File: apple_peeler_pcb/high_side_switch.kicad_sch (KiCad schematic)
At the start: 7 parts, among them Q7 2N7002, Q8 AO3401A

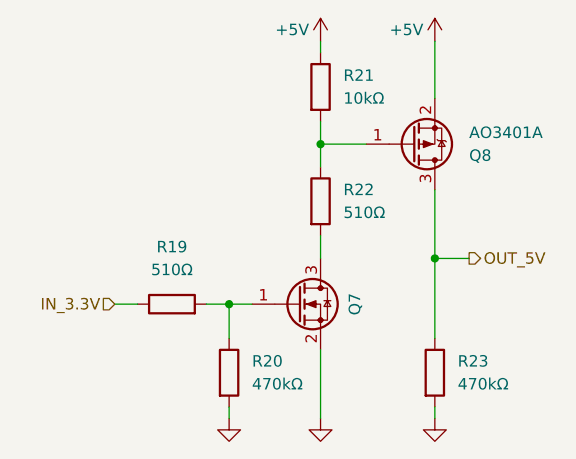
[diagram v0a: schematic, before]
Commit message: we paid for all the pins, we're gonna use all the pins
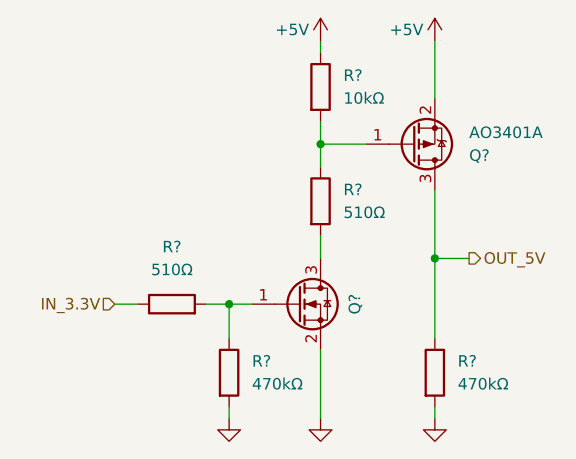
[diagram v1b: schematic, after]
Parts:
- renumbered Q8 to Q?, Q7 to Q?, R21 to R?, R22 to R?, R19 to R?, R23 to R?, R20 to R?
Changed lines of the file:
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@@
 		(on_board yes)
 		(dnp no)
-		(property "Reference" "#PWR044"
+		(property "Reference" "#PWR0106"
 			(at 153.67 128.27 0)
 			(effects
@@
 		(instances
 			(project "apple_peeler_pcb"
-				(path "/d5946b96-44a8-4a28-8641-19803e1510af/ab4760da-4146-4688-a275-418314974b55/6046dcba-ade8-41f9-96d2-caaf24154fd4"
-					(reference "#PWR044")
+				(path "/d5946b96-44a8-4a28-8641-19803e1510af/ab4760da-4146-4688-a275-418314974b55/207d6e2c-5657-4cae-9098-bf31bbf0eeb3/3e7a2019-c147-43be-8925-3656ede786af"
+					(reference "#PWR050")
+					(unit 1)
+				)
+				(path "/d5946b96-44a8-4a28-8641-19803e1510af/ab4760da-4146-4688-a275-418314974b55/216077bc-1e97-451f-9a4f-0a4e0691e85e/3e7a2019-c147-43be-8925-3656ede786af"
+					(reference "#PWR0106")
 					(unit 1)
 				)
@@
 		(on_board yes)
 		(dnp no)
-		(property "Reference" "#PWR043"
+		(property "Reference" "#PWR0105"
 			(at 153.67 83.82 0)
 			(effects
@@
 		(instances
 			(project "apple_peeler_pcb"
-				(path "/d5946b96-44a8-4a28-8641-19803e1510af/ab4760da-4146-4688-a275-418314974b55/6046dcba-ade8-41f9-96d2-caaf24154fd4"
-					(reference "#PWR043")
+				(path "/d5946b96-44a8-4a28-8641-19803e1510af/ab4760da-4146-4688-a275-418314974b55/207d6e2c-5657-4cae-9098-bf31bbf0eeb3/3e7a2019-c147-43be-8925-3656ede786af"
+					(reference "#PWR049")
+					(unit 1)
+				)
+				(path "/d5946b96-44a8-4a28-8641-19803e1510af/ab4760da-4146-4688-a275-418314974b55/216077bc-1e97-451f-9a4f-0a4e0691e85e/3e7a2019-c147-43be-8925-3656ede786af"
+					(reference "#PWR0105")
 					(unit 1)
 				)
@@
 		(dnp no)
 		(fields_autoplaced yes)
-		(property "Reference" "R21"
+		(property "Reference" "R?"
 			(at 143.51 83.8199 0)
 			(effects
@@
 		(instances
 			(project "apple_peeler_pcb"
-				(path "/d5946b96-44a8-4a28-8641-19803e1510af/ab4760da-4146-4688-a275-418314974b55/6046dcba-ade8-41f9-96d2-caaf24154fd4"
-					(reference "R21")
+				(path "/d5946b96-44a8-4a28-8641-19803e1510af/ab4760da-4146-4688-a275-418314974b55/207d6e2c-5657-4cae-9098-bf31bbf0eeb3/3e7a2019-c147-43be-8925-3656ede786af"
+					(reference "R?")
+					(unit 1)
+				)
+				(path "/d5946b96-44a8-4a28-8641-19803e1510af/ab4760da-4146-4688-a275-418314974b55/216077bc-1e97-451f-9a4f-0a4e0691e85e/3e7a2019-c147-43be-8925-3656ede786af"
+					(reference "R?")
 					(unit 1)
 				)
@@
 		(on_board yes)
 		(dnp no)
-		(property "Reference" "#PWR041"
+		(property "Reference" "#PWR0100"
 			(at 140.97 83.82 0)
 			(effects
@@
 		(instances
 			(project "apple_peeler_pcb"
-				(path "/d5946b96-44a8-4a28-8641-19803e1510af/ab4760da-4146-4688-a275-418314974b55/6046dcba-ade8-41f9-96d2-caaf24154fd4"
-					(reference "#PWR041")
+				(path "/d5946b96-44a8-4a28-8641-19803e1510af/ab4760da-4146-4688-a275-418314974b55/207d6e2c-5657-4cae-9098-bf31bbf0eeb3/3e7a2019-c147-43be-8925-3656ede786af"
+					(reference "#PWR044")
+					(unit 1)
+				)
+				(path "/d5946b96-44a8-4a28-8641-19803e1510af/ab4760da-4146-4688-a275-418314974b55/216077bc-1e97-451f-9a4f-0a4e0691e85e/3e7a2019-c147-43be-8925-3656ede786af"
+					(reference "#PWR0100")
 					(unit 1)
 				)
@@
 		(dnp no)
 		(fields_autoplaced yes)
-		(property "Reference" "R22"
+		(property "Reference" "R?"
 			(at 143.51 96.5199 0)
 			(effects
@@
 		(instances
 			(project "apple_peeler_pcb"
-				(path "/d5946b96-44a8-4a28-8641-19803e1510af/ab4760da-4146-4688-a275-418314974b55/6046dcba-ade8-41f9-96d2-caaf24154fd4"
-					(reference "R22")
+				(path "/d5946b96-44a8-4a28-8641-19803e1510af/ab4760da-4146-4688-a275-418314974b55/207d6e2c-5657-4cae-9098-bf31bbf0eeb3/3e7a2019-c147-43be-8925-3656ede786af"
+					(reference "R?")
+					(unit 1)
+				)
+				(path "/d5946b96-44a8-4a28-8641-19803e1510af/ab4760da-4146-4688-a275-418314974b55/216077bc-1e97-451f-9a4f-0a4e0691e85e/3e7a2019-c147-43be-8925-3656ede786af"
+					(reference "R?")
 					(unit 1)
 				)
@@
 		(dnp no)
 		(fields_autoplaced yes)
-		(property "Reference" "R19"
+		(property "Reference" "R?"
 			(at 124.46 102.87 90)
 			(effects
@@
 		(instances
 			(project "apple_peeler_pcb"
-				(path "/d5946b96-44a8-4a28-8641-19803e1510af/ab4760da-4146-4688-a275-418314974b55/6046dcba-ade8-41f9-96d2-caaf24154fd4"
-					(reference "R19")
+				(path "/d5946b96-44a8-4a28-8641-19803e1510af/ab4760da-4146-4688-a275-418314974b55/207d6e2c-5657-4cae-9098-bf31bbf0eeb3/3e7a2019-c147-43be-8925-3656ede786af"
+					(reference "R?")
+					(unit 1)
+				)
+				(path "/d5946b96-44a8-4a28-8641-19803e1510af/ab4760da-4146-4688-a275-418314974b55/216077bc-1e97-451f-9a4f-0a4e0691e85e/3e7a2019-c147-43be-8925-3656ede786af"
+					(reference "R?")
 					(unit 1)
 				)
@@
 		(on_board yes)
 		(dnp no)
-		(property "Reference" "#PWR042"
+		(property "Reference" "#PWR0101"
 			(at 140.97 128.27 0)
 			(effects
@@
 		(instances
 			(project "apple_peeler_pcb"
-				(path "/d5946b96-44a8-4a28-8641-19803e1510af/ab4760da-4146-4688-a275-418314974b55/6046dcba-ade8-41f9-96d2-caaf24154fd4"
-					(reference "#PWR042")
+				(path "/d5946b96-44a8-4a28-8641-19803e1510af/ab4760da-4146-4688-a275-418314974b55/207d6e2c-5657-4cae-9098-bf31bbf0eeb3/3e7a2019-c147-43be-8925-3656ede786af"
+					(reference "#PWR048")
+					(unit 1)
+				)
+				(path "/d5946b96-44a8-4a28-8641-19803e1510af/ab4760da-4146-4688-a275-418314974b55/216077bc-1e97-451f-9a4f-0a4e0691e85e/3e7a2019-c147-43be-8925-3656ede786af"
+					(reference "#PWR0101")
 					(unit 1)
 				)
@@
 		(on_board yes)
 		(dnp no)
-		(property "Reference" "#PWR040"
+		(property "Reference" "#PWR099"
 			(at 130.81 128.27 0)
 			(effects
@@
 		(instances
 			(project "apple_peeler_pcb"
-				(path "/d5946b96-44a8-4a28-8641-19803e1510af/ab4760da-4146-4688-a275-418314974b55/6046dcba-ade8-41f9-96d2-caaf24154fd4"
-					(reference "#PWR040")
+				(path "/d5946b96-44a8-4a28-8641-19803e1510af/ab4760da-4146-4688-a275-418314974b55/207d6e2c-5657-4cae-9098-bf31bbf0eeb3/3e7a2019-c147-43be-8925-3656ede786af"
+					(reference "#PWR043")
+					(unit 1)
+				)
+				(path "/d5946b96-44a8-4a28-8641-19803e1510af/ab4760da-4146-4688-a275-418314974b55/216077bc-1e97-451f-9a4f-0a4e0691e85e/3e7a2019-c147-43be-8925-3656ede786af"
+					(reference "#PWR099")
 					(unit 1)
 				)
@@
 		(dnp no)
 		(fields_autoplaced yes)
-		(property "Reference" "R23"
+		(property "Reference" "R?"
 			(at 156.21 115.5699 0)
 			(effects
@@
 		(instances
 			(project "apple_peeler_pcb"
-				(path "/d5946b96-44a8-4a28-8641-19803e1510af/ab4760da-4146-4688-a275-418314974b55/6046dcba-ade8-41f9-96d2-caaf24154fd4"
-					(reference "R23")
+				(path "/d5946b96-44a8-4a28-8641-19803e1510af/ab4760da-4146-4688-a275-418314974b55/207d6e2c-5657-4cae-9098-bf31bbf0eeb3/3e7a2019-c147-43be-8925-3656ede786af"
+					(reference "R?")
+					(unit 1)
+				)
+				(path "/d5946b96-44a8-4a28-8641-19803e1510af/ab4760da-4146-4688-a275-418314974b55/216077bc-1e97-451f-9a4f-0a4e0691e85e/3e7a2019-c147-43be-8925-3656ede786af"
+					(reference "R?")
 					(unit 1)
 				)
@@
 		(on_board yes)
 		(dnp no)
-		(property "Reference" "Q8"
+		(property "Reference" "Q?"
 			(at 157.48 92.7101 0)
 			(effects
@@
 		(instances
 			(project "apple_peeler_pcb"
-				(path "/d5946b96-44a8-4a28-8641-19803e1510af/ab4760da-4146-4688-a275-418314974b55/6046dcba-ade8-41f9-96d2-caaf24154fd4"
-					(reference "Q8")
+				(path "/d5946b96-44a8-4a28-8641-19803e1510af/ab4760da-4146-4688-a275-418314974b55/207d6e2c-5657-4cae-9098-bf31bbf0eeb3/3e7a2019-c147-43be-8925-3656ede786af"
+					(reference "Q?")
+					(unit 1)
+				)
+				(path "/d5946b96-44a8-4a28-8641-19803e1510af/ab4760da-4146-4688-a275-418314974b55/216077bc-1e97-451f-9a4f-0a4e0691e85e/3e7a2019-c147-43be-8925-3656ede786af"
+					(reference "Q?")
 					(unit 1)
 				)
@@
 		(on_board yes)
 		(dnp no)
-		(property "Reference" "Q7"
+		(property "Reference" "Q?"
 			(at 144.78 109.22 90)
 			(effects
@@
 		(instances
 			(project "apple_peeler_pcb"
-				(path "/d5946b96-44a8-4a28-8641-19803e1510af/ab4760da-4146-4688-a275-418314974b55/6046dcba-ade8-41f9-96d2-caaf24154fd4"
-					(reference "Q7")
+				(path "/d5946b96-44a8-4a28-8641-19803e1510af/ab4760da-4146-4688-a275-418314974b55/207d6e2c-5657-4cae-9098-bf31bbf0eeb3/3e7a2019-c147-43be-8925-3656ede786af"
+					(reference "Q?")
+					(unit 1)
+				)
+				(path "/d5946b96-44a8-4a28-8641-19803e1510af/ab4760da-4146-4688-a275-418314974b55/216077bc-1e97-451f-9a4f-0a4e0691e85e/3e7a2019-c147-43be-8925-3656ede786af"
+					(reference "Q?")
 					(unit 1)
 				)
@@
 		(dnp no)
 		(fields_autoplaced yes)
-		(property "Reference" "R20"
+		(property "Reference" "R?"
 			(at 133.35 115.5699 0)
 			(effects
@@
 		(instances
 			(project "apple_peeler_pcb"
-				(path "/d5946b96-44a8-4a28-8641-19803e1510af/ab4760da-4146-4688-a275-418314974b55/6046dcba-ade8-41f9-96d2-caaf24154fd4"
-					(reference "R20")
-					(unit 1)
-				)
+				(path "/d5946b96-44a8-4a28-8641-19803e1510af/ab4760da-4146-4688-a275-418314974b55/207d6e2c-5657-4cae-9098-bf31bbf0eeb3/3e7a2019-c147-43be-8925-3656ede786af"
+					(reference "R?")
+					(unit 1)
+				)
+				(path "/d5946b96-44a8-4a28-8641-19803e1510af/ab4760da-4146-4688-a275-418314974b55/216077bc-1e97-451f-9a4f-0a4e0691e85e/3e7a2019-c147-43be-8925-3656ede786af"
+					(reference "R?")
+					(unit 1)
+				)

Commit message: use wleds instead of individual leds
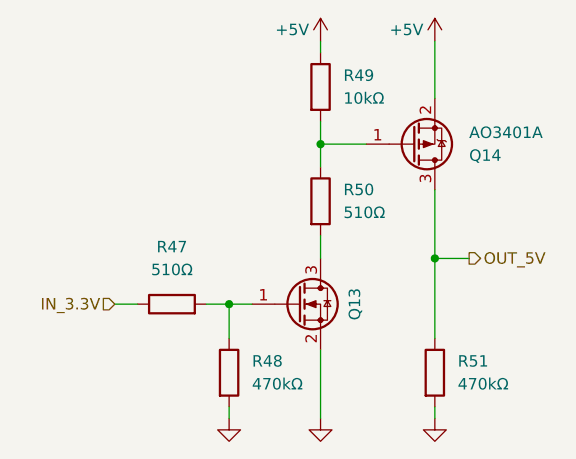
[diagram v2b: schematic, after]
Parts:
- gave numbers to parts that had none: 7
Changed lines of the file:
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@@
 		(on_board yes)
 		(dnp no)
-		(property "Reference" "#PWR0106"
+		(property "Reference" "#PWR0102"
 			(at 153.67 128.27 0)
 			(effects
@@
 			(project "apple_peeler_pcb"
 				(path "/d5946b96-44a8-4a28-8641-19803e1510af/ab4760da-4146-4688-a275-418314974b55/207d6e2c-5657-4cae-9098-bf31bbf0eeb3/3e7a2019-c147-43be-8925-3656ede786af"
-					(reference "#PWR050")
-					(unit 1)
-				)
-				(path "/d5946b96-44a8-4a28-8641-19803e1510af/ab4760da-4146-4688-a275-418314974b55/216077bc-1e97-451f-9a4f-0a4e0691e85e/3e7a2019-c147-43be-8925-3656ede786af"
-					(reference "#PWR0106")
+					(reference "#PWR0107")
+					(unit 1)
+				)
+				(path "/d5946b96-44a8-4a28-8641-19803e1510af/ab4760da-4146-4688-a275-418314974b55/216077bc-1e97-451f-9a4f-0a4e0691e85e/3e7a2019-c147-43be-8925-3656ede786af"
+					(reference "#PWR0102")
 					(unit 1)
 				)
@@
 		(on_board yes)
 		(dnp no)
-		(property "Reference" "#PWR0105"
+		(property "Reference" "#PWR0101"
 			(at 153.67 83.82 0)
 			(effects
@@
 			(project "apple_peeler_pcb"
 				(path "/d5946b96-44a8-4a28-8641-19803e1510af/ab4760da-4146-4688-a275-418314974b55/207d6e2c-5657-4cae-9098-bf31bbf0eeb3/3e7a2019-c147-43be-8925-3656ede786af"
-					(reference "#PWR049")
-					(unit 1)
-				)
-				(path "/d5946b96-44a8-4a28-8641-19803e1510af/ab4760da-4146-4688-a275-418314974b55/216077bc-1e97-451f-9a4f-0a4e0691e85e/3e7a2019-c147-43be-8925-3656ede786af"
-					(reference "#PWR0105")
+					(reference "#PWR0106")
+					(unit 1)
+				)
+				(path "/d5946b96-44a8-4a28-8641-19803e1510af/ab4760da-4146-4688-a275-418314974b55/216077bc-1e97-451f-9a4f-0a4e0691e85e/3e7a2019-c147-43be-8925-3656ede786af"
+					(reference "#PWR0101")
 					(unit 1)
 				)
@@
 		(dnp no)
 		(fields_autoplaced yes)
-		(property "Reference" "R?"
+		(property "Reference" "R49"
 			(at 143.51 83.8199 0)
 			(effects
@@
 			(project "apple_peeler_pcb"
 				(path "/d5946b96-44a8-4a28-8641-19803e1510af/ab4760da-4146-4688-a275-418314974b55/207d6e2c-5657-4cae-9098-bf31bbf0eeb3/3e7a2019-c147-43be-8925-3656ede786af"
-					(reference "R?")
-					(unit 1)
-				)
-				(path "/d5946b96-44a8-4a28-8641-19803e1510af/ab4760da-4146-4688-a275-418314974b55/216077bc-1e97-451f-9a4f-0a4e0691e85e/3e7a2019-c147-43be-8925-3656ede786af"
-					(reference "R?")
+					(reference "R54")
+					(unit 1)
+				)
+				(path "/d5946b96-44a8-4a28-8641-19803e1510af/ab4760da-4146-4688-a275-418314974b55/216077bc-1e97-451f-9a4f-0a4e0691e85e/3e7a2019-c147-43be-8925-3656ede786af"
+					(reference "R49")
 					(unit 1)
 				)
@@
 		(on_board yes)
 		(dnp no)
-		(property "Reference" "#PWR0100"
+		(property "Reference" "#PWR099"
 			(at 140.97 83.82 0)
 			(effects
@@
 			(project "apple_peeler_pcb"
 				(path "/d5946b96-44a8-4a28-8641-19803e1510af/ab4760da-4146-4688-a275-418314974b55/207d6e2c-5657-4cae-9098-bf31bbf0eeb3/3e7a2019-c147-43be-8925-3656ede786af"
-					(reference "#PWR044")
-					(unit 1)
-				)
-				(path "/d5946b96-44a8-4a28-8641-19803e1510af/ab4760da-4146-4688-a275-418314974b55/216077bc-1e97-451f-9a4f-0a4e0691e85e/3e7a2019-c147-43be-8925-3656ede786af"
-					(reference "#PWR0100")
+					(reference "#PWR0104")
+					(unit 1)
+				)
+				(path "/d5946b96-44a8-4a28-8641-19803e1510af/ab4760da-4146-4688-a275-418314974b55/216077bc-1e97-451f-9a4f-0a4e0691e85e/3e7a2019-c147-43be-8925-3656ede786af"
+					(reference "#PWR099")
 					(unit 1)
 				)
@@
 		(dnp no)
 		(fields_autoplaced yes)
-		(property "Reference" "R?"
+		(property "Reference" "R50"
 			(at 143.51 96.5199 0)
 			(effects
@@
 			(project "apple_peeler_pcb"
 				(path "/d5946b96-44a8-4a28-8641-19803e1510af/ab4760da-4146-4688-a275-418314974b55/207d6e2c-5657-4cae-9098-bf31bbf0eeb3/3e7a2019-c147-43be-8925-3656ede786af"
-					(reference "R?")
-					(unit 1)
-				)
-				(path "/d5946b96-44a8-4a28-8641-19803e1510af/ab4760da-4146-4688-a275-418314974b55/216077bc-1e97-451f-9a4f-0a4e0691e85e/3e7a2019-c147-43be-8925-3656ede786af"
-					(reference "R?")
+					(reference "R55")
+					(unit 1)
+				)
+				(path "/d5946b96-44a8-4a28-8641-19803e1510af/ab4760da-4146-4688-a275-418314974b55/216077bc-1e97-451f-9a4f-0a4e0691e85e/3e7a2019-c147-43be-8925-3656ede786af"
+					(reference "R50")
 					(unit 1)
 				)
@@
 		(dnp no)
 		(fields_autoplaced yes)
-		(property "Reference" "R?"
+		(property "Reference" "R47"
 			(at 124.46 102.87 90)
 			(effects
@@
 			(project "apple_peeler_pcb"
 				(path "/d5946b96-44a8-4a28-8641-19803e1510af/ab4760da-4146-4688-a275-418314974b55/207d6e2c-5657-4cae-9098-bf31bbf0eeb3/3e7a2019-c147-43be-8925-3656ede786af"
-					(reference "R?")
-					(unit 1)
-				)
-				(path "/d5946b96-44a8-4a28-8641-19803e1510af/ab4760da-4146-4688-a275-418314974b55/216077bc-1e97-451f-9a4f-0a4e0691e85e/3e7a2019-c147-43be-8925-3656ede786af"
-					(reference "R?")
+					(reference "R52")
+					(unit 1)
+				)
+				(path "/d5946b96-44a8-4a28-8641-19803e1510af/ab4760da-4146-4688-a275-418314974b55/216077bc-1e97-451f-9a4f-0a4e0691e85e/3e7a2019-c147-43be-8925-3656ede786af"
+					(reference "R47")
 					(unit 1)
 				)
@@
 		(on_board yes)
 		(dnp no)
-		(property "Reference" "#PWR0101"
+		(property "Reference" "#PWR0100"
 			(at 140.97 128.27 0)
 			(effects
@@
 			(project "apple_peeler_pcb"
 				(path "/d5946b96-44a8-4a28-8641-19803e1510af/ab4760da-4146-4688-a275-418314974b55/207d6e2c-5657-4cae-9098-bf31bbf0eeb3/3e7a2019-c147-43be-8925-3656ede786af"
-					(reference "#PWR048")
-					(unit 1)
-				)
-				(path "/d5946b96-44a8-4a28-8641-19803e1510af/ab4760da-4146-4688-a275-418314974b55/216077bc-1e97-451f-9a4f-0a4e0691e85e/3e7a2019-c147-43be-8925-3656ede786af"
-					(reference "#PWR0101")
+					(reference "#PWR0105")
+					(unit 1)
+				)
+				(path "/d5946b96-44a8-4a28-8641-19803e1510af/ab4760da-4146-4688-a275-418314974b55/216077bc-1e97-451f-9a4f-0a4e0691e85e/3e7a2019-c147-43be-8925-3656ede786af"
+					(reference "#PWR0100")
 					(unit 1)
 				)
@@
 		(on_board yes)
 		(dnp no)
-		(property "Reference" "#PWR099"
+		(property "Reference" "#PWR098"
 			(at 130.81 128.27 0)
 			(effects
@@
 			(project "apple_peeler_pcb"
 				(path "/d5946b96-44a8-4a28-8641-19803e1510af/ab4760da-4146-4688-a275-418314974b55/207d6e2c-5657-4cae-9098-bf31bbf0eeb3/3e7a2019-c147-43be-8925-3656ede786af"
-					(reference "#PWR043")
-					(unit 1)
-				)
-				(path "/d5946b96-44a8-4a28-8641-19803e1510af/ab4760da-4146-4688-a275-418314974b55/216077bc-1e97-451f-9a4f-0a4e0691e85e/3e7a2019-c147-43be-8925-3656ede786af"
-					(reference "#PWR099")
+					(reference "#PWR0103")
+					(unit 1)
+				)
+				(path "/d5946b96-44a8-4a28-8641-19803e1510af/ab4760da-4146-4688-a275-418314974b55/216077bc-1e97-451f-9a4f-0a4e0691e85e/3e7a2019-c147-43be-8925-3656ede786af"
+					(reference "#PWR098")
 					(unit 1)
 				)
@@
 		(dnp no)
 		(fields_autoplaced yes)
-		(property "Reference" "R?"
+		(property "Reference" "R51"
 			(at 156.21 115.5699 0)
 			(effects
@@
 			(project "apple_peeler_pcb"
 				(path "/d5946b96-44a8-4a28-8641-19803e1510af/ab4760da-4146-4688-a275-418314974b55/207d6e2c-5657-4cae-9098-bf31bbf0eeb3/3e7a2019-c147-43be-8925-3656ede786af"
-					(reference "R?")
-					(unit 1)
-				)
-				(path "/d5946b96-44a8-4a28-8641-19803e1510af/ab4760da-4146-4688-a275-418314974b55/216077bc-1e97-451f-9a4f-0a4e0691e85e/3e7a2019-c147-43be-8925-3656ede786af"
-					(reference "R?")
+					(reference "R56")
+					(unit 1)
+				)
+				(path "/d5946b96-44a8-4a28-8641-19803e1510af/ab4760da-4146-4688-a275-418314974b55/216077bc-1e97-451f-9a4f-0a4e0691e85e/3e7a2019-c147-43be-8925-3656ede786af"
+					(reference "R51")
 					(unit 1)
 				)
@@
 		(on_board yes)
 		(dnp no)
-		(property "Reference" "Q?"
+		(property "Reference" "Q14"
 			(at 157.48 92.7101 0)
 			(effects
@@
 			(project "apple_peeler_pcb"
 				(path "/d5946b96-44a8-4a28-8641-19803e1510af/ab4760da-4146-4688-a275-418314974b55/207d6e2c-5657-4cae-9098-bf31bbf0eeb3/3e7a2019-c147-43be-8925-3656ede786af"
-					(reference "Q?")
-					(unit 1)
-				)
-				(path "/d5946b96-44a8-4a28-8641-19803e1510af/ab4760da-4146-4688-a275-418314974b55/216077bc-1e97-451f-9a4f-0a4e0691e85e/3e7a2019-c147-43be-8925-3656ede786af"
-					(reference "Q?")
+					(reference "Q16")
+					(unit 1)
+				)
+				(path "/d5946b96-44a8-4a28-8641-19803e1510af/ab4760da-4146-4688-a275-418314974b55/216077bc-1e97-451f-9a4f-0a4e0691e85e/3e7a2019-c147-43be-8925-3656ede786af"
+					(reference "Q14")
 					(unit 1)
 				)
@@
 		(on_board yes)
 		(dnp no)
-		(property "Reference" "Q?"
+		(property "Reference" "Q13"
 			(at 144.78 109.22 90)
 			(effects
@@
 			(project "apple_peeler_pcb"
 				(path "/d5946b96-44a8-4a28-8641-19803e1510af/ab4760da-4146-4688-a275-418314974b55/207d6e2c-5657-4cae-9098-bf31bbf0eeb3/3e7a2019-c147-43be-8925-3656ede786af"
-					(reference "Q?")
-					(unit 1)
-				)
-				(path "/d5946b96-44a8-4a28-8641-19803e1510af/ab4760da-4146-4688-a275-418314974b55/216077bc-1e97-451f-9a4f-0a4e0691e85e/3e7a2019-c147-43be-8925-3656ede786af"
-					(reference "Q?")
+					(reference "Q15")
+					(unit 1)
+				)
+				(path "/d5946b96-44a8-4a28-8641-19803e1510af/ab4760da-4146-4688-a275-418314974b55/216077bc-1e97-451f-9a4f-0a4e0691e85e/3e7a2019-c147-43be-8925-3656ede786af"
+					(reference "Q13")
 					(unit 1)
 				)
@@
 		(dnp no)
 		(fields_autoplaced yes)
-		(property "Reference" "R?"
+		(property "Reference" "R48"
 			(at 133.35 115.5699 0)
 			(effects
@@
 			(project "apple_peeler_pcb"
 				(path "/d5946b96-44a8-4a28-8641-19803e1510af/ab4760da-4146-4688-a275-418314974b55/207d6e2c-5657-4cae-9098-bf31bbf0eeb3/3e7a2019-c147-43be-8925-3656ede786af"
-					(reference "R?")
-					(unit 1)
-				)
-				(path "/d5946b96-44a8-4a28-8641-19803e1510af/ab4760da-4146-4688-a275-418314974b55/216077bc-1e97-451f-9a4f-0a4e0691e85e/3e7a2019-c147-43be-8925-3656ede786af"
-					(reference "R?")
-					(unit 1)
-				)
+					(reference "R53")
+					(unit 1)
+				)
+				(path "/d5946b96-44a8-4a28-8641-19803e1510af/ab4760da-4146-4688-a275-418314974b55/216077bc-1e97-451f-9a4f-0a4e0691e85e/3e7a2019-c147-43be-8925-3656ede786af"
+					(reference "R48")
+					(unit 1)
+				)
